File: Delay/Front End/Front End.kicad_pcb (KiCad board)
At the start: 2 copper layers, 50.5 x 104.5 mm, 11 parts, among them J1 AudioJack2_SwitchT, J2 AudioJack2_SwitchT, J3 AudioJack2_SwitchT, J4 Conn_01x14_Socket

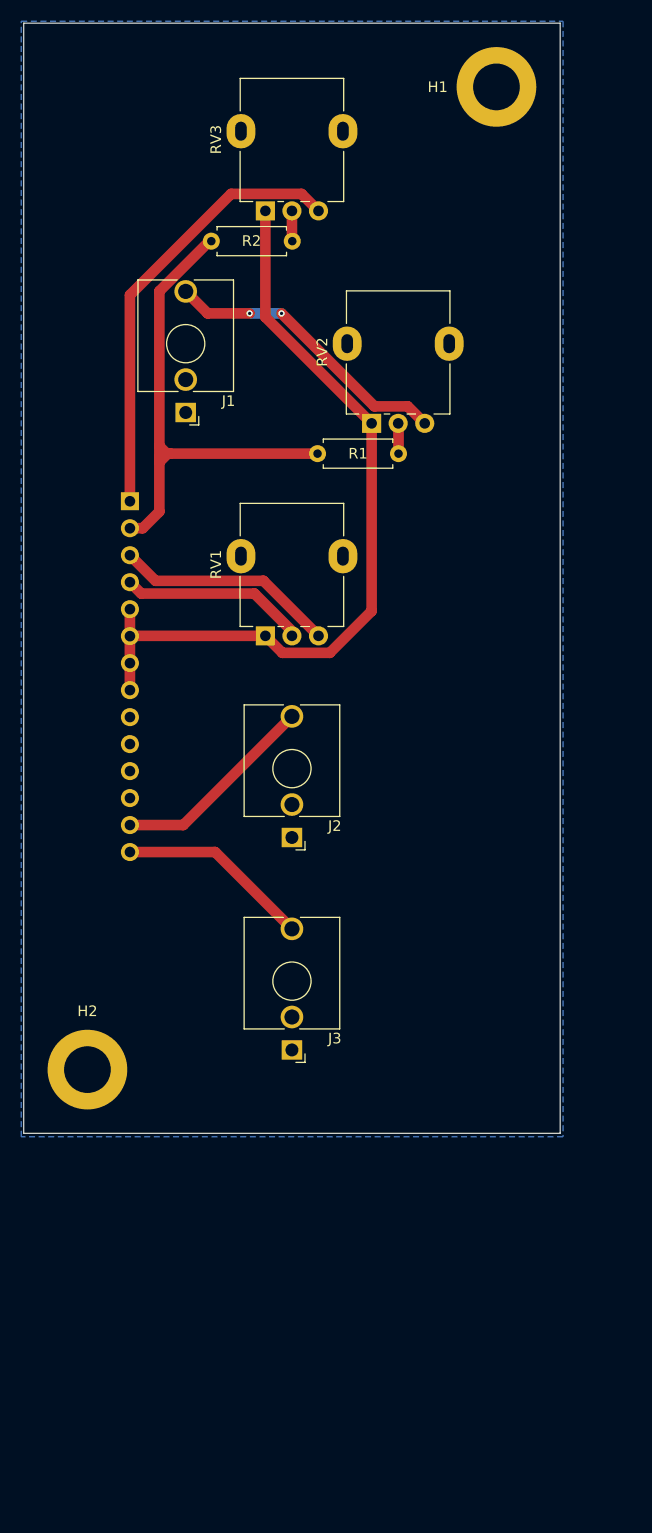
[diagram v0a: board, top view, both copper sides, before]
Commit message: Finish diode ladder filter
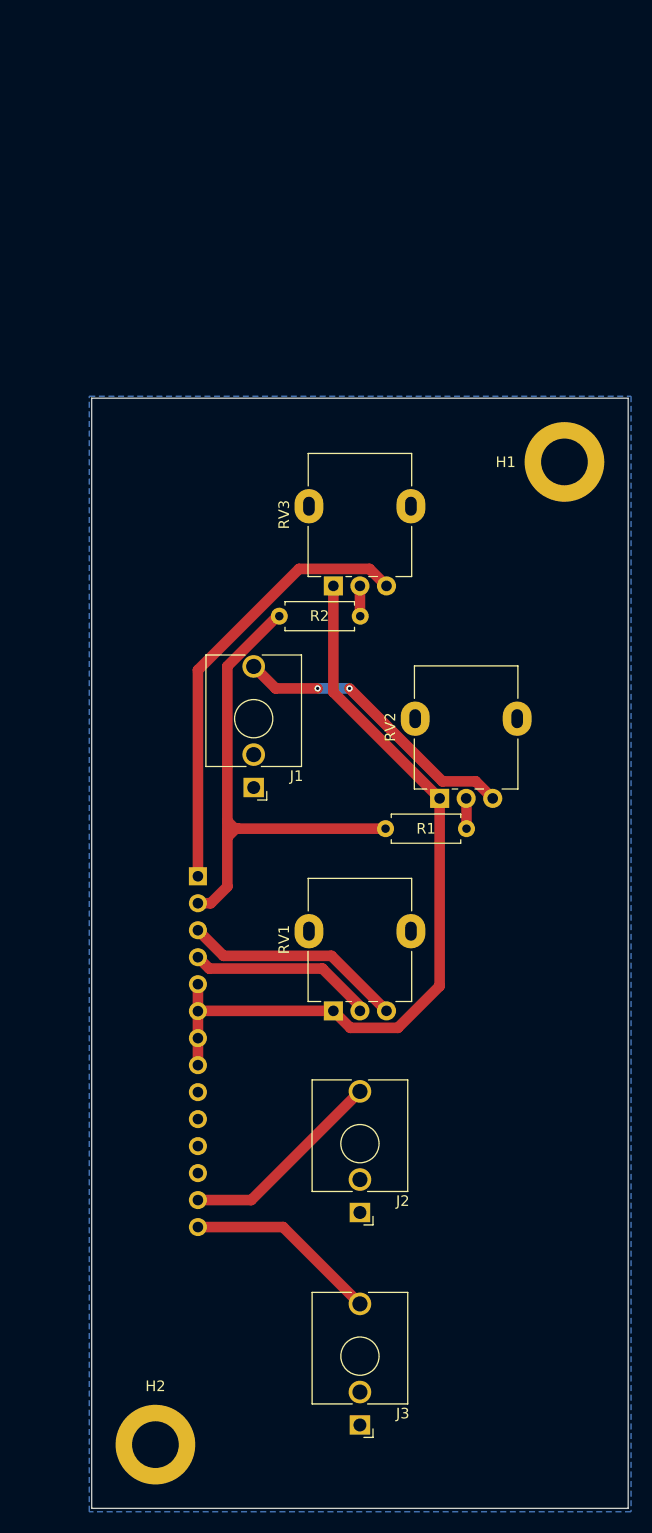
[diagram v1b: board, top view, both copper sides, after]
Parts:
- moved RV1 35.9 mm to (147.9, 102.7)
- moved J4 35.9 mm to (135.1, 90.0)
- moved RV2 35.9 mm to (157.9, 82.7)
- moved H1 35.9 mm to (169.6, 51.0)
- moved J1 35.9 mm to (140.4, 81.6)
- moved J2 35.9 mm to (150.4, 121.6)
- moved J3 35.9 mm to (150.4, 141.6)
- moved R1 35.9 mm to (152.8, 85.5)
- moved R2 35.9 mm to (142.8, 65.5)
- moved RV3 35.9 mm to (147.9, 62.6)
- moved H2 35.9 mm to (131.1, 143.5)
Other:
- board text added: "JLCJLCJLCJLC"
